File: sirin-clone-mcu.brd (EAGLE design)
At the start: 101.6 x 57.1 mm, 55 parts, among them J1 PJ-002A, J3 30_PIN_CONNECTOR_MALE, J5 SWITCHCRAFT_PHONEJACK, J6 SWD_CONNECTOR, T2 MCP1825S, U4 SGTL5000_32QFN, U5 23LC1024

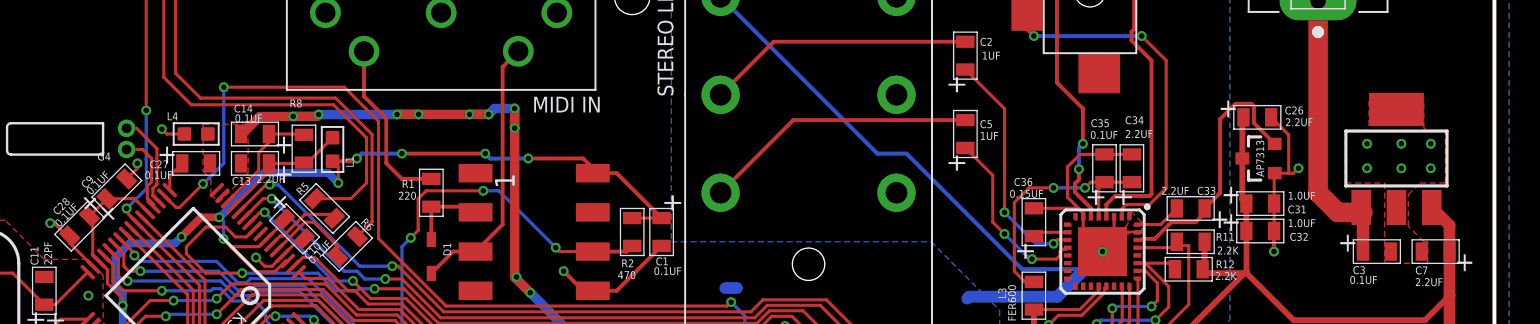
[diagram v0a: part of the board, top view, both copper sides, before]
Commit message: placed bom order
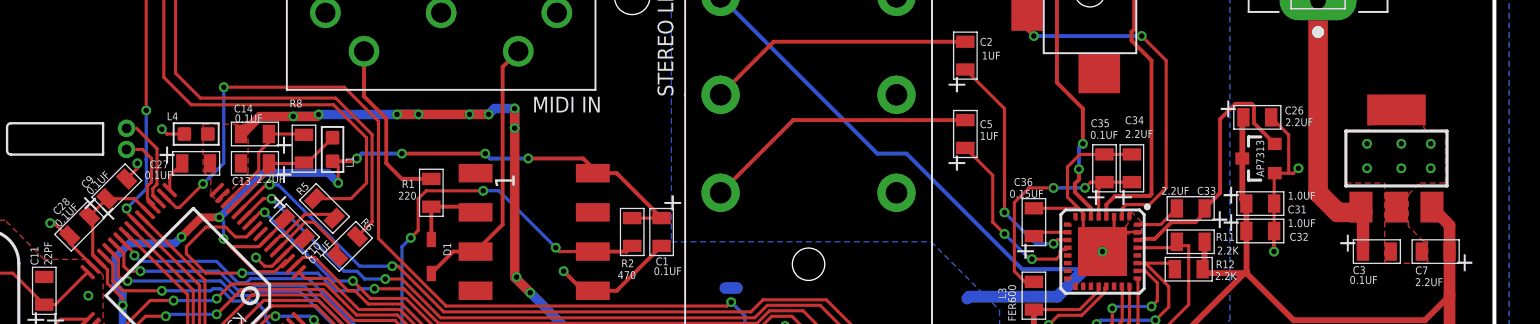
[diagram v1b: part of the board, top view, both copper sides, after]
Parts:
- D6: device moon-germs-v1:SOT23-3 -> moon-germs-v1_main:SOT23-3
- J5: device moon-germs-v1_main:STEREO_JACK_2SWITCH -> sirin-clone-library:STEREO_JACK_2SWITCH
- T2: device moon-germs-v1_main:SOT-223 -> sirin-clone-library:SOT223
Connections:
- net GND: now also T2.4; no longer T2.PAD
